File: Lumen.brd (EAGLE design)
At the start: 59.3 x 24 mm, 33 parts, among them J1 AVR_SPI_PRG_6PTH, U1 Tiny45-20-SMT, Y1 8Mhz

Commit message: Minor layout updates for new production order.
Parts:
- R6, R8: device BlueRobotics-Main:C0402 -> BlueRobotics-Main:R0402
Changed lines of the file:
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@@
 <element name="C7" library="resistor" package="C0603" value="NP" x="46.625" y="19" rot="R180"/>
 <element name="R7" library="resistor" package="R1206" value="NP" x="45.875" y="21.125" rot="R180"/>
-<element name="R6" library="BlueRobotics-Main" package="C0402" value="15K 1/5W" x="32.25" y="11.25" rot="R180"/>
-<element name="R8" library="BlueRobotics-Main" package="C0402" value="300K" x="33.875" y="13.25" rot="R270"/>
+<element name="R6" library="BlueRobotics-Main" package="R0402" value="15K 1/5W" x="32.25" y="11.25" rot="R180"/>
+<element name="R8" library="BlueRobotics-Main" package="R0402" value="300K" x="33.875" y="13.25" rot="R270"/>
 <element name="Y1" library="SparkFun" package="RESONATOR-SMD" value="8Mhz" x="36.875" y="12.625"/>
 </elements>

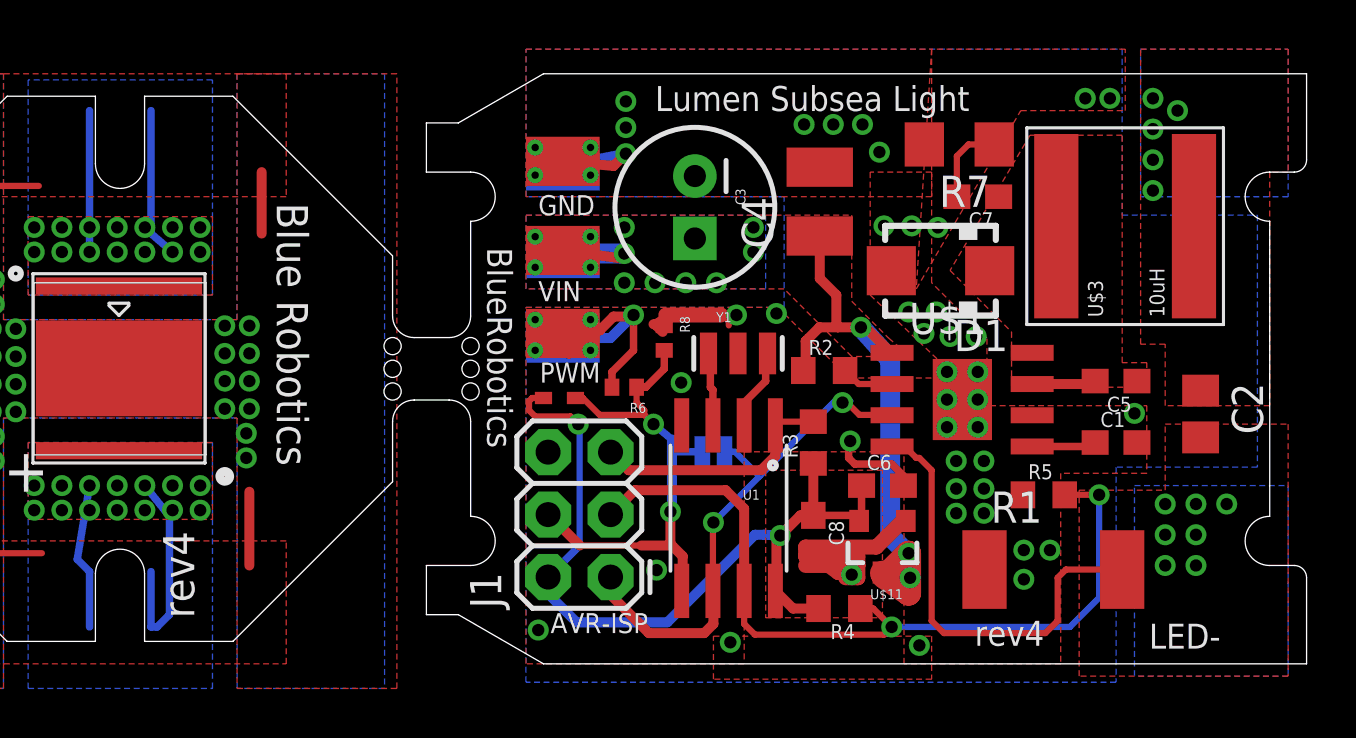
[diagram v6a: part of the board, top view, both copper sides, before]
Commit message: Rev6 as produced with IDC connector.
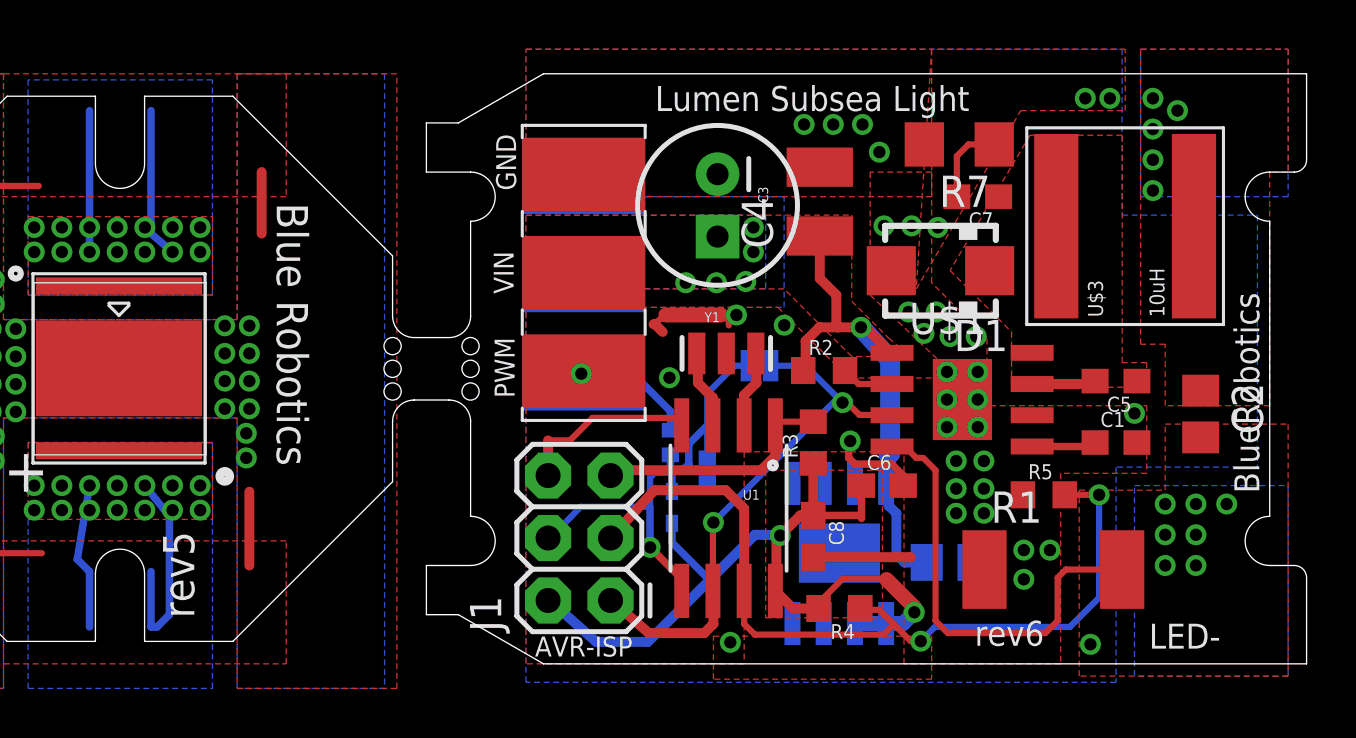
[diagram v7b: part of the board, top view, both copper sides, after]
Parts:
- removed U$4, U$5, U$6, U$7, U$8, U$9: PAD2X3MM, BlueRobotics-Main:PAD-2X3MM
- added C9: 0.18uF 50V, resistor:C0805
- added U$12: 009176003032006, BlueRobotics-Main:AVX-9176-3POS
- added U$13: RT9068-3.3V, BlueRobotics-Main:SOIC8N-LJ
- J1: value AVR_SPI_PRG_6PTH -> AVR_SPI
- U$11: value VREG-ZXTR2105 -> 009176003032006; device BlueRobotics-Main:SOT23-3 -> BlueRobotics-Main:AVX-9176-3POS
- moved U$11 19.4 mm to (30.6, 19.9), turned to 270 degrees
- moved D2 6.45 mm to (34.2, 6.31), flipped to the bottom, turned to 90 degrees
- moved R8 5.65 mm to (35.6, 7.88), flipped to the bottom, turned to 90 degrees
- moved SJ1 3.97 mm to (37.8, 12.1)
- moved R6 2.93 mm to (34.1, 9.00), flipped to the bottom, turned to 90 degrees
- moved J1 0.95 mm to (31.7, 2.58)
- moved C3 0.93 mm to (36.0, 18.6)
- moved Y1 0.48 mm to (36.4, 12.6)
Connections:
- net GND: now also C9.2, U$12.1, U$13.5, U$13.6, U$13.7, U$13.PAD; no longer U$6.P$1, U$9.P$1
- net SIGNAL_HV: now also U$11.3, U$12.3; no longer U$4.P$1, U$7.P$1
- net VCC: now also U$13.1, U$13.2; no longer U$11.2
- net VIN: now also C9.1, U$11.2, U$12.2, U$13.8; no longer U$11.3, U$5.P$1, U$8.P$1
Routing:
- net VIN: track 32.6 -> 22.4 mm, vias 15 -> 6
- net SIGNAL_HV: track 15.8 -> 6.00 mm, vias 5 -> 1
- net GND: track 25.9 -> 19.0 mm, vias 46 -> 35
- net SIGNAL: track 21.2 -> 19.8 mm, vias 2 -> 1
- net TEMP: track 33.3 -> 34.3 mm
- net LED-PWM: track 22.3 -> 22.9 mm
- net LED-: vias 7 -> 8
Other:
- board text added: "R.J. 9/17"
- board text added: "rev5"
- board text added: "rev6"
- board text removed: "R.J. 12/15"
- board text removed: "rev4"

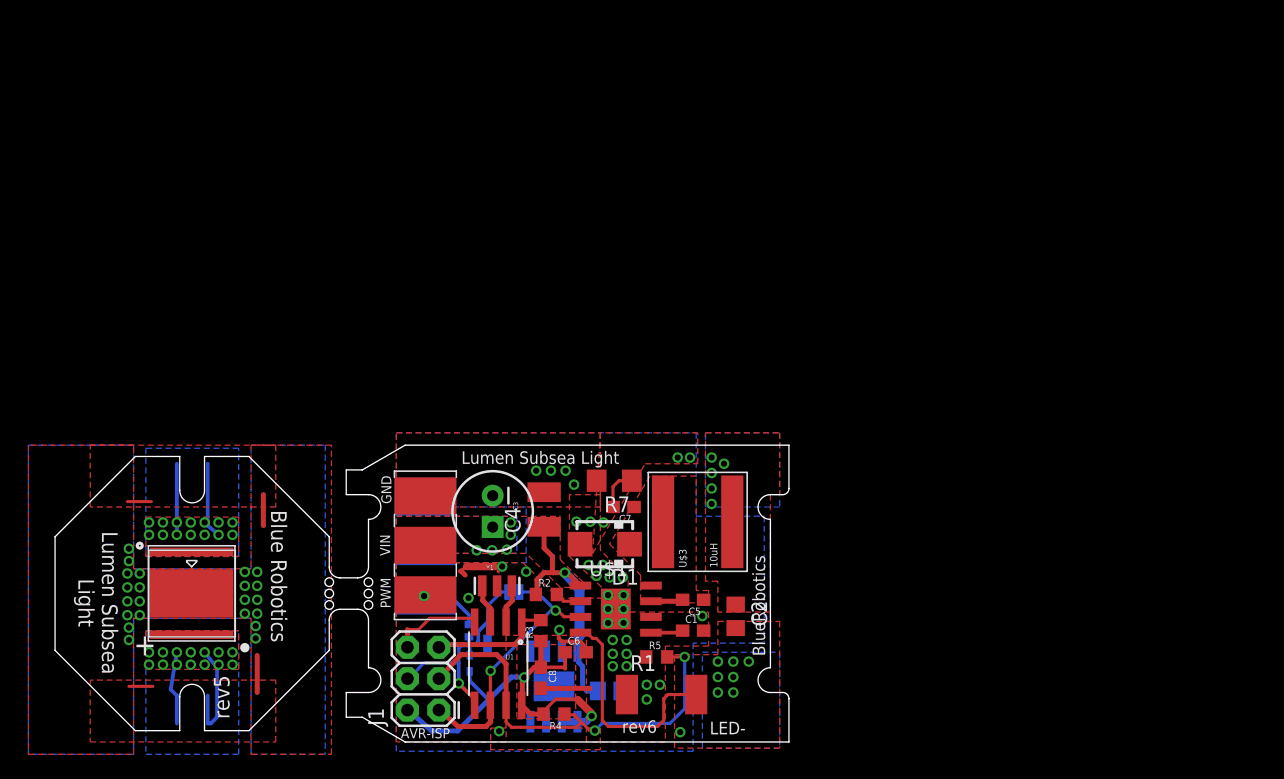
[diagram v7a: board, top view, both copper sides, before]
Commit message: Re-layout board for new size. In progress.
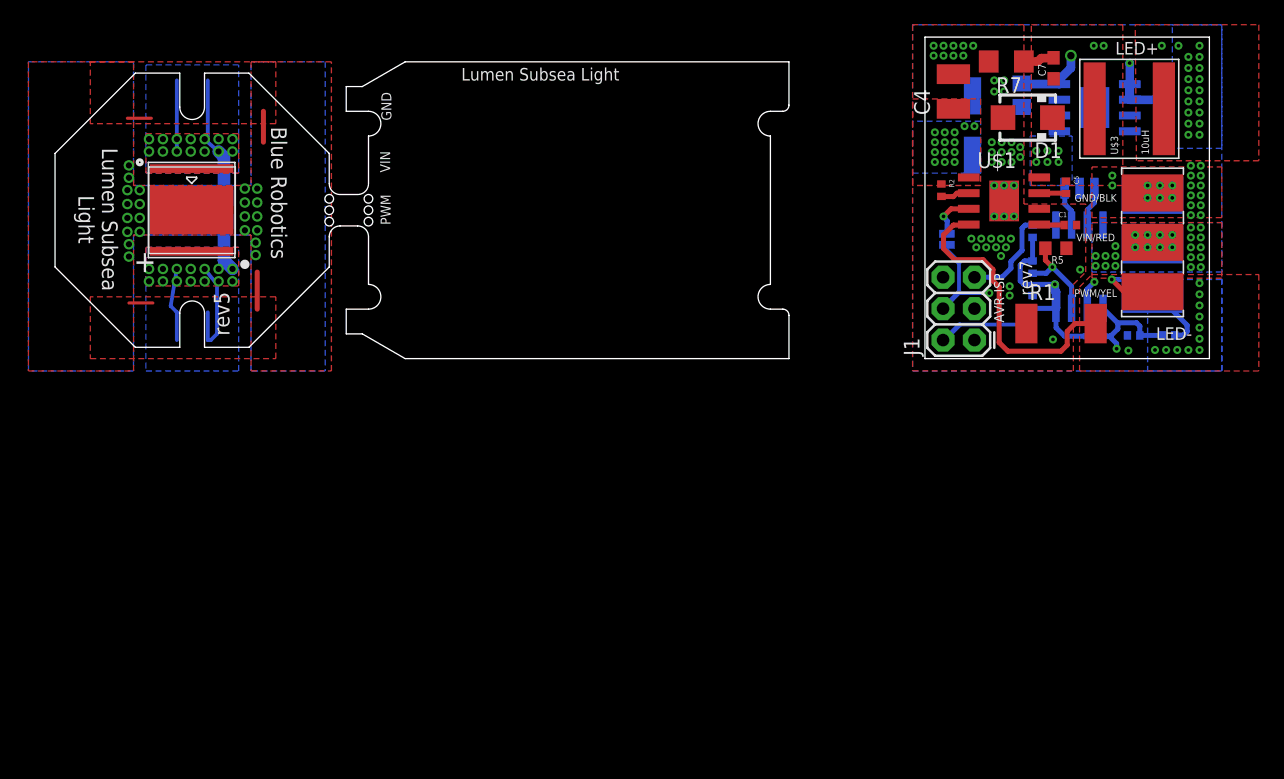
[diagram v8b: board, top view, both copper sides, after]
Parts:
- removed R3: 10K, resistor:R0603
- added R9: 3.3K 1%, BlueRobotics-Main:R0402
- C1, C5, C8: device resistor:C0603 -> BlueRobotics-Main:C0402
- C3: device SparkFun-Capacitors:CPOL-RADIAL-100UF-25V -> SparkFun-Capacitors:PANASONIC_D
- J1: value AVR_SPI -> AVR_SPI_PRG_6PTH
- R2: device resistor:R0603 -> BlueRobotics-Main:R0402
- R4: value 3.3K 1% -> 10K; device resistor:R0603 -> BlueRobotics-Main:R0402
- moved C6 65.8 mm to (90.2, 52.9), flipped to the bottom, turned to 90 degrees
- moved U$13 64.0 mm to (84.7, 51.3), turned to 270 degrees
- moved U$11 63.7 mm to (89.4, 44.4)
- moved U$12 63.7 mm to (89.4, 44.2)
- moved R6 61.4 mm to (90.7, 32.9), turned to 180 degrees
- moved C9 58.6 mm to (78.8, 52.3), turned to 270 degrees
- moved R8 57.9 mm to (87.9, 32.9), turned to 180 degrees
- moved D2 57.1 mm to (84.7, 32.8), turned to 180 degrees
- moved Y1 57.0 mm to (83.5, 44.8), flipped to the bottom
- moved U1 56.9 mm to (83.5, 38.4), flipped to the bottom
- moved R4 55.0 mm to (79.7, 41.3), flipped to the bottom, turned to 90 degrees
- moved C2 52.9 mm to (14.3, 43.0), flipped to the bottom, turned to 90 degrees
- moved J1 52.6 mm to (75.0, 32.5)
- moved C8 50.1 mm to (79.7, 35.6), flipped to the bottom, turned to 90 degrees
- moved C3 49.8 mm to (74.8, 49.8), flipped to the bottom
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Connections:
- net GND: now also C3.-; no longer C3.2
- net LED+: no longer C2.1
- net LED+ISO: now also C2.2
- net LED-: no longer C2.2
- net LED-ISO: now also C2.1
- net RESET: now also R4.2; no longer R3.2
- net TEMP: now also R9.1; no longer R4.1
- net VCC: now also R4.1, R9.2; no longer R3.1, R4.2
- net VIN: now also C3.+; no longer C3.1
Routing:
- net TEMP: track 34.3 -> 15.2 mm, vias 2 -> 1
- net GND: track 19.0 -> 0.00 mm, vias 35 -> 68
- net VCC: track 34.0 -> 51.7 mm
- net VIN: track 22.4 -> 7.15 mm, vias 6 -> 40
- net SIGNAL: track 19.8 -> 32.7 mm, vias 1 -> 2
- net SIGNAL_HV: track 6.00 -> 13.0 mm
- net LED-PWM: track 22.9 -> 28.9 mm
- net LED-: track 18.4 -> 24.0 mm, vias 8 -> 11
- net LED-ISO: track 14.8 -> 18.9 mm
- net LED+ISO: track 11.9 -> 15.8 mm
- net N$2: track 3.37 -> 2.53 mm
- net VCC6211: track 2.63 -> 2.03 mm
- added copper zone on layer 15, net EXT
- added copper zone on layer 2, net EXT
- added copper zone on layer 15, net GND
- added copper zone on layer 16, net N$5
- added copper zone on layer 2, net VIN
- removed copper zone on layer 1, net VCC
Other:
- board size 59.3 x 24 mm -> 93.3 x 26 mm
- board text added: "GND/BLK"
- board text added: "PWM/YEL"
- board text added: "R.J. 1/18"
- board text added: "VIN/RED"
- board text added: "rev7"
- board text removed: "R.J. 9/17"
- board text removed: "rev6"
